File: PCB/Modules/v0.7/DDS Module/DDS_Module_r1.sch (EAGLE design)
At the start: 38 parts, among them IC1 SN65HVD31DR, IC2 LM3480-5.0, IC3 AD9834, IC4 SN65HVD31DR, IC5 AD5620BRJZ-2500RL7, J1 BNCPTH, Y1 ASE10MHZ

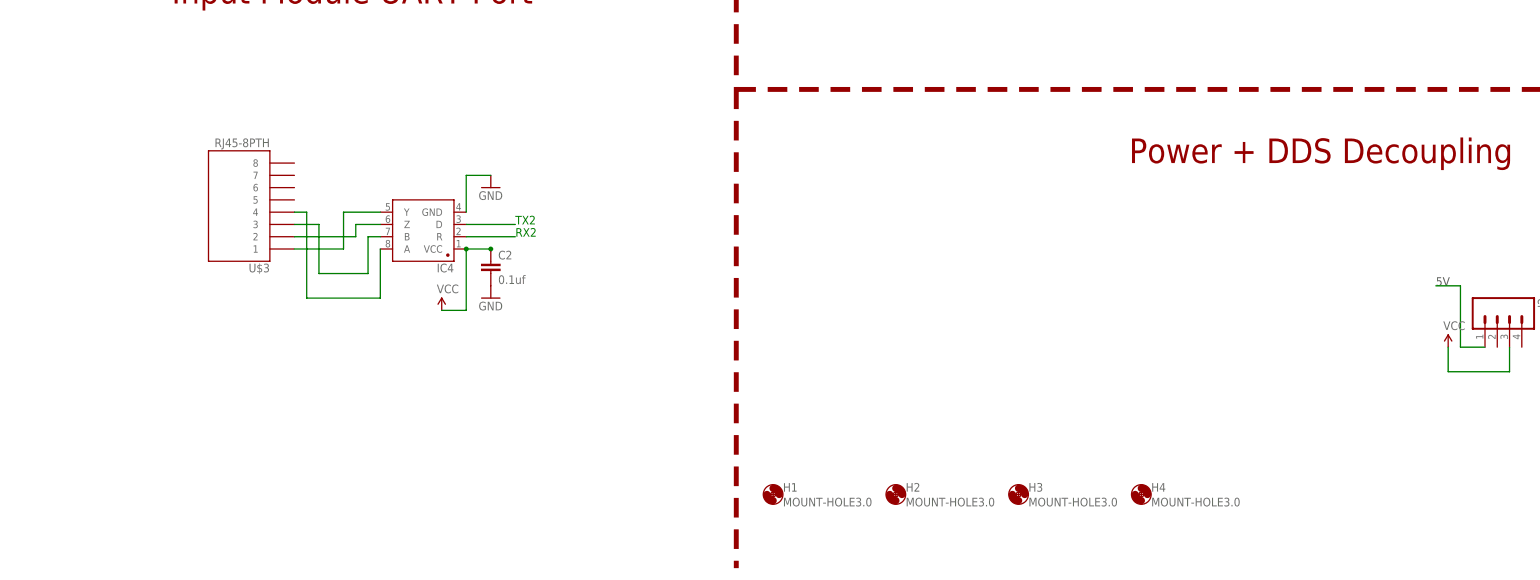
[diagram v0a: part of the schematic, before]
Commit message: -Added SNES Module PCB design -Added SNES Module bottom-guard design -Added DDS Module enclosure -Updated link to Bpod-CAD repository in schematic files
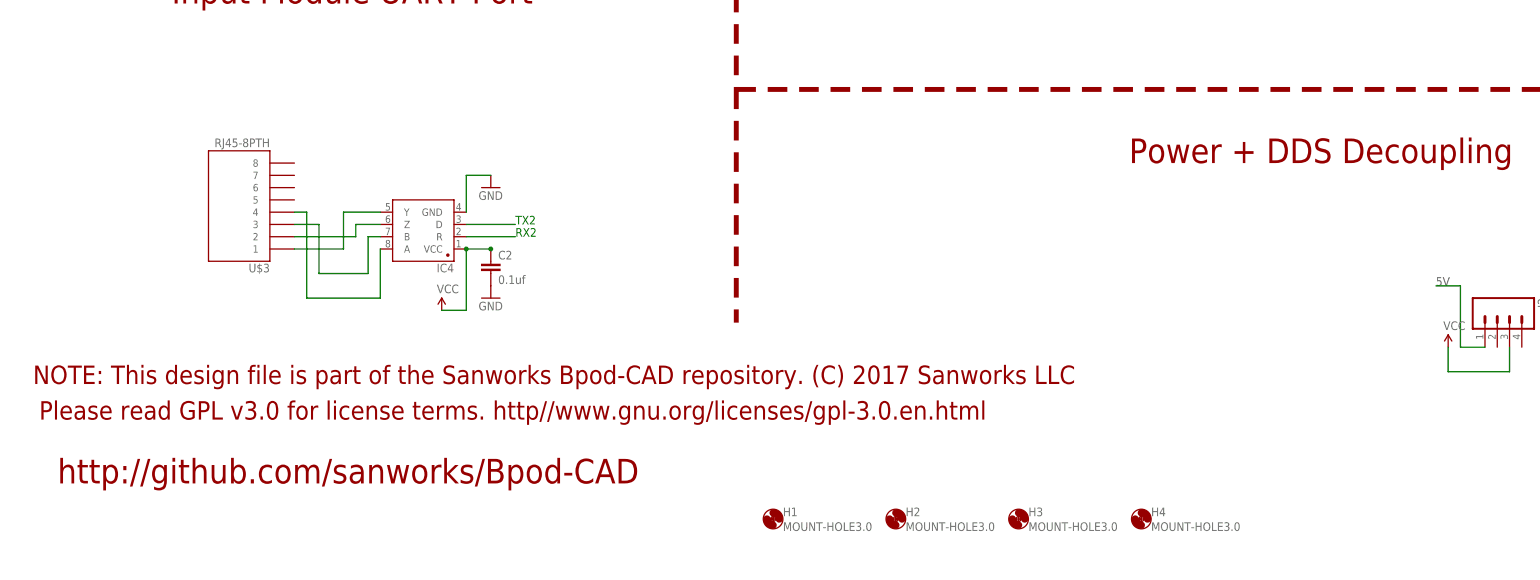
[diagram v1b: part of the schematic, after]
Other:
- note added: "NOTE: This design file is part of the Sanworks Bpod-CAD repository. (C) 2017 Sanworks LLC"
- note added: "Please read GPL v3.0 for license terms. http//www.gnu.org/licenses/gpl-3.0.en.html"
- note added: "http://github.com/sanworks/Bpod-CAD"
- moved on the sheet: H1, H2, H3, H4
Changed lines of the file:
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@@
 <wire x1="20.32" y1="236.22" x2="20.32" y2="114.3" width="1.016" layer="94" style="longdash"/>
 <wire x1="20.32" y1="114.3" x2="20.32" y2="81.28" width="1.016" layer="94" style="longdash"/>
-<wire x1="20.32" y1="81.28" x2="20.32" y2="-17.78" width="1.016" layer="94" style="longdash"/>
+<wire x1="20.32" y1="81.28" x2="20.32" y2="33.02" width="1.016" layer="94" style="longdash"/>
 <wire x1="20.32" y1="114.3" x2="-129.54" y2="114.3" width="1.016" layer="94" style="longdash"/>
 <text x="-116.84" y="223.52" size="5.08" layer="94">Bpod State Machine UART Port + Power</text>
@@
 <wire x1="20.32" y1="81.28" x2="248.92" y2="81.28" width="1.016" layer="94" style="longdash"/>
 <text x="101.6" y="66.04" size="5.08" layer="94">Power + DDS Decoupling</text>
+<text x="-123.952" y="12.954" size="3.81" layer="94" font="vector">Please read GPL v3.0 for license terms. http//www.gnu.org/licenses/gpl-3.0.en.html</text>
+<text x="-125.222" y="20.32" size="3.81" layer="94" font="vector">NOTE: This design file is part of the Sanworks Bpod-CAD repository. (C) 2017 Sanworks LLC</text>
+<text x="-120.142" y="-0.254" size="5.08" layer="94" font="vector">http://github.com/sanworks/Bpod-CAD</text>
 </plain>
 <instances>
@@
 <instance part="J7" gate="G$1" x="-33.02" y="195.58" rot="R180"/>
 <instance part="J5" gate="G$1" x="-12.7" y="157.48" rot="R90"/>
-<instance part="H1" gate="G$1" x="27.94" y="-2.54"/>
-<instance part="H2" gate="G$1" x="53.34" y="-2.54"/>
-<instance part="H3" gate="G$1" x="78.74" y="-2.54"/>
-<instance part="H4" gate="G$1" x="104.14" y="-2.54"/>
+<instance part="H1" gate="G$1" x="27.94" y="-7.62"/>
+<instance part="H2" gate="G$1" x="53.34" y="-7.62"/>
+<instance part="H3" gate="G$1" x="78.74" y="-7.62"/>
+<instance part="H4" gate="G$1" x="104.14" y="-7.62"/>
 <instance part="J6" gate="G$1" x="-73.66" y="200.66" rot="R270"/>
 <instance part="IC2" gate="G$1" x="-99.06" y="198.12"/>
